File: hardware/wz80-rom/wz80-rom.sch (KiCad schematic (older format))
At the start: 6 parts, among them J1 CONN_01X32, SW1 SW_DIP_x02, U1 SST39SF010, U2 74LS32

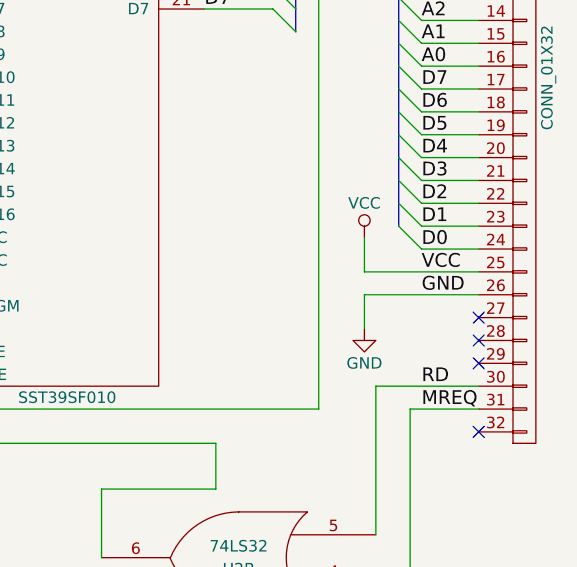
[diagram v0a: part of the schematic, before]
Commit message: Moved schematics into hardware/. Added start of software.
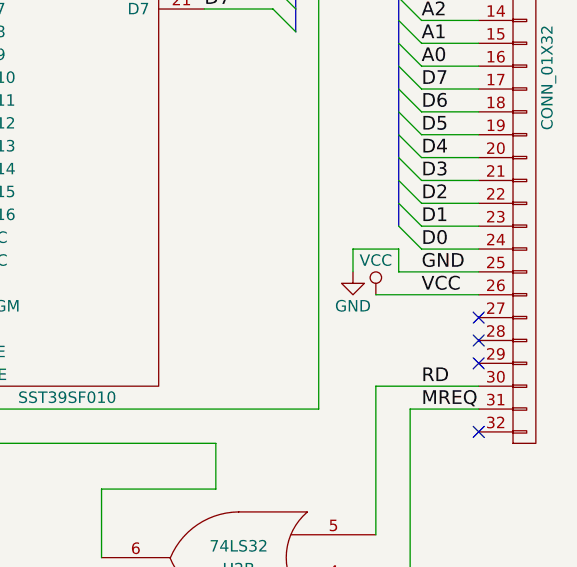
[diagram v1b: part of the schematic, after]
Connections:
- net GND: now also J1.25 (P25); no longer J1.26 (P26)
- net VCC: now also J1.26 (P26); no longer J1.25 (P25)
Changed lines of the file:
@@
-	1    0    0    -1
-$EndComp
-$Comp
-L VCC #PWR04
-U 1 1 58D01F5D
-P 6800 4450
-F 0 "#PWR04" H 6800 4300 50  0001 C CNN
-F 1 "VCC" H 6800 4600 50  0000 C CNN
-F 2 "" H 6800 4450 50  0001 C CNN
-F 3 "" H 6800 4450 50  0001 C CNN
-	1    6800 4450
-	1    0    0    -1
-$EndComp
-$Comp
-L GND #PWR05
-U 1 1 58D01F7F
-P 6800 4850
-F 0 "#PWR05" H 6800 4600 50  0001 C CNN
-F 1 "GND" H 6800 4700 50  0000 C CNN
-F 2 "" H 6800 4850 50  0001 C CNN
-F 3 "" H 6800 4850 50  0001 C CNN
-	1    6800 4850
 	1    0    0    -1
 $EndComp
@@
 	7050 4500 7300 4500
 Wire Wire Line
-	6800 4600 7300 4600
-Wire Wire Line
-	6800 4700 7300 4700
-Wire Wire Line
 	6850 5100 7300 5100
 Wire Wire Line
@@
 Wire Wire Line
 	4750 4750 4900 4750
-Wire Wire Line
-	6800 4600 6800 4450
-Wire Wire Line
-	6800 4700 6800 4850
 Wire Wire Line
 	6600 2150 7250 2150
@@
 Text Label 7050 5200 0    60   ~ 0
 MREQ
+Text Label 7050 4700 0    60   ~ 0
+VCC
 Text Label 7050 4600 0    60   ~ 0
-VCC
-Text Label 7050 4700 0    60   ~ 0
 GND
 Text Label 4700 4250 0    60   ~ 0
@@
 Wire Wire Line
 	4250 4750 3900 4750
+Wire Wire Line
+	6950 4600 7300 4600
+Wire Wire Line
+	6850 4700 7300 4700
+$Comp
+L VCC #PWR?
+U 1 1 58D04BFB
+P 6850 4700
+F 0 "#PWR?" H 6850 4550 50  0001 C CNN
+F 1 "VCC" H 6850 4850 50  0000 C CNN
+F 2 "" H 6850 4700 50  0001 C CNN
+F 3 "" H 6850 4700 50  0001 C CNN
+	1    6850 4700
+	1    0    0    -1
+$EndComp
+$Comp
+L GND #PWR?
+U 1 1 58D04C1B
+P 6750 4600
+F 0 "#PWR?" H 6750 4350 50  0001 C CNN
+F 1 "GND" H 6750 4450 50  0000 C CNN
+F 2 "" H 6750 4600 50  0001 C CNN
+F 3 "" H 6750 4600 50  0001 C CNN
+	1    6750 4600
+	1    0    0    -1
+$EndComp
+Wire Wire Line
+	6950 4600 6950 4500
+Wire Wire Line
+	6950 4500 6750 4500
+Wire Wire Line
+	6750 4500 6750 4600
 $EndSCHEMATC
